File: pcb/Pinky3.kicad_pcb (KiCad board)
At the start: 2 copper layers, 137 x 100.9 mm, 67 parts, among them J1 MJ-4PP-9, P1 i2c-pin, P2 i2c-pin, SW1 RESET_SW, SW10 SW_PUSH, SW11 SW_PUSH, SW12 SW_PUSH, SW13 SW_PUSH, SW14 SW_PUSH, SW15 SW_PUSH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

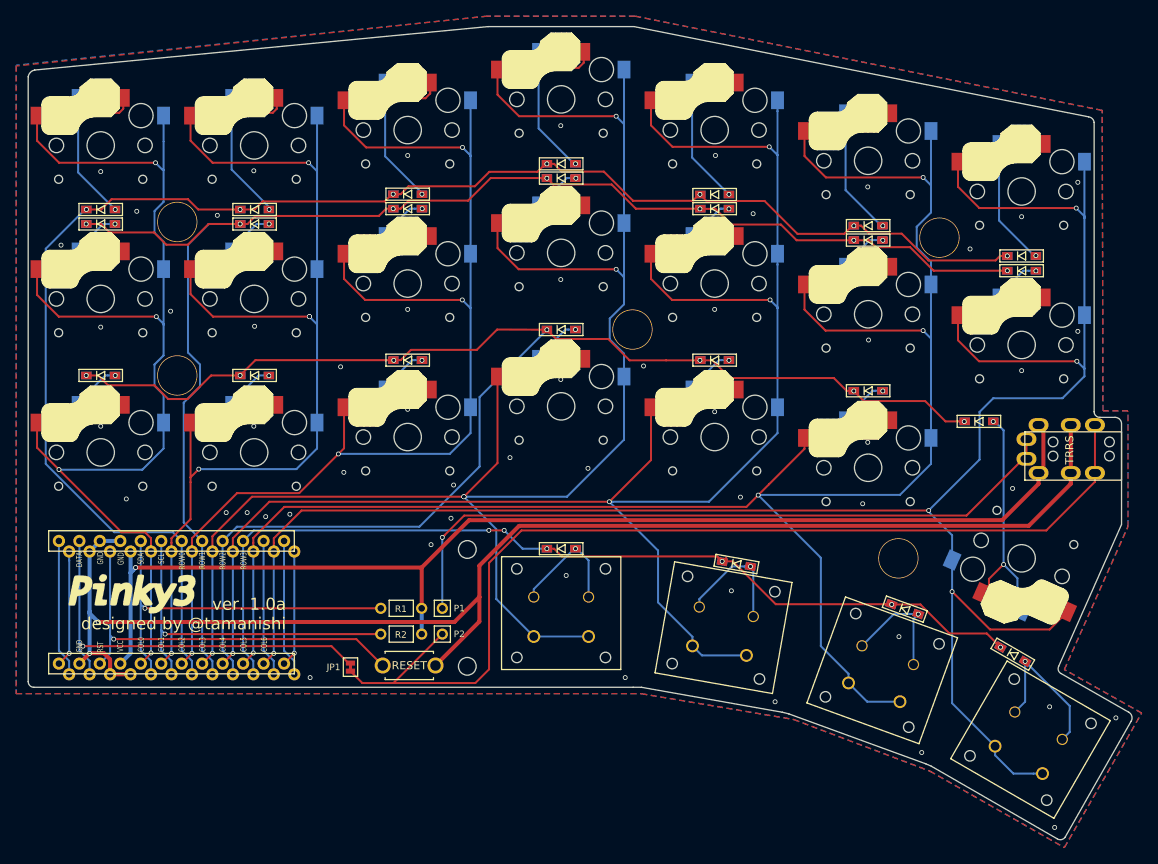
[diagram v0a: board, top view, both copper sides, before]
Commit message: - change thumb switches to Kailh PG1232.
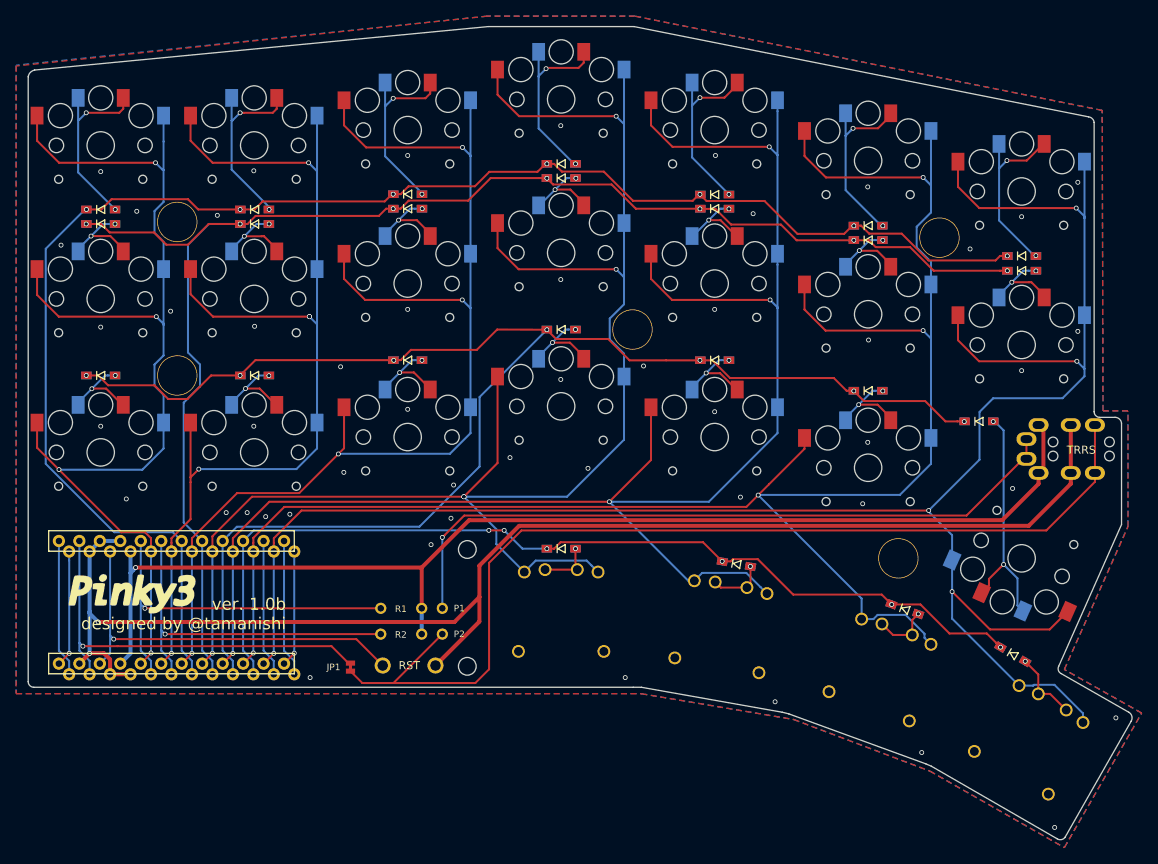
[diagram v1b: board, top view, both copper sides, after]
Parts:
- SW10, SW11, SW12, SW13, SW15, SW16, SW17, SW19, SW2, SW20, SW21, SW23, SW24, SW25, SW3, SW4, SW5, SW6, SW7, SW8, SW9: footprint kbd:Choc_Hotswap -> lib:Choc_Hotswap
- SW14, SW18, SW22, SW26: footprint lib:Kailh-PG1425-X-Switch-reversible -> lib:kailh_low_choc
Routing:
- net Net-(D25-Pad2): track 19.2 -> 9.00 mm
- net Net-(D17-Pad2): track 15.4 -> 7.03 mm
- net Net-(D13-Pad2): track 15.0 -> 7.03 mm
- net Net-(D21-Pad2): track 15.1 -> 7.24 mm
- net col3: track 204.8 -> 200.5 mm
- net col4: track 214.4 -> 210.1 mm
- net col5: track 232.2 -> 228.2 mm
- net col6: track 253.8 -> 250.1 mm
- net GND: vias 57 -> 53
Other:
- board text added: "ver. 1.0b designed by @tamanishi"
- board text removed: "ver. 1.0a designed by @tamanishi"

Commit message: supports choc v2
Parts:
- SW10, SW11, SW12, SW13, SW15, SW16, SW17, SW19, SW2, SW20, SW21, SW23, SW24, SW25, SW3, SW4, SW5, SW6, SW7, SW8, SW9: footprint lib:Choc_Hotswap -> lib:Choc_v2_Hotswap
- SW14, SW18, SW22, SW26: footprint lib:kailh_low_choc -> lib:Choc_v2_Hotswap
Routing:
- net col6: track 250.1 -> 271.8 mm, vias 5 -> 6
- net col3: track 200.5 -> 218.1 mm
- net col4: track 210.1 -> 225.8 mm, vias 4 -> 5
- net Net-(D13-Pad2): track 7.03 -> 22.1 mm, vias 1 -> 2
- net Net-(D21-Pad2): track 7.24 -> 22.1 mm, vias 1 -> 2
- net col5: track 228.2 -> 242.5 mm, vias 4 -> 5
- net Net-(D17-Pad2): track 7.03 -> 21.1 mm, vias 1 -> 2
- net Net-(D25-Pad2): track 9.00 -> 21.7 mm, vias 1 -> 2
- net Net-(D24-Pad2): track 29.8 -> 34.8 mm
- net col2: track 144.2 -> 145.4 mm
- net col1: track 130.7 -> 131.7 mm, vias 5 -> 4
- net GND: vias 53 -> 50
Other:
- board text added: "ver. 1.0c designed by @tamanishi"
- board text removed: "ver. 1.0b designed by @tamanishi"

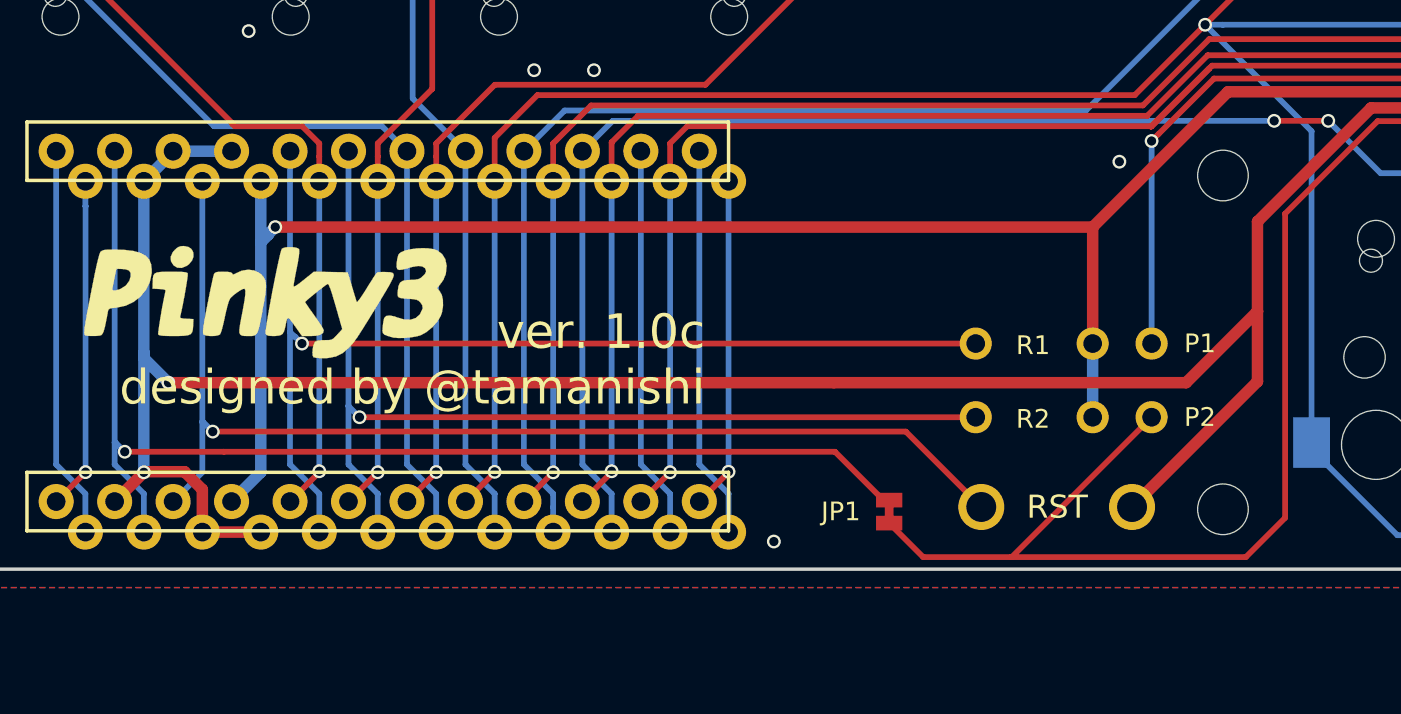
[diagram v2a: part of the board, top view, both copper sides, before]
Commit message: change horizontal reset switch
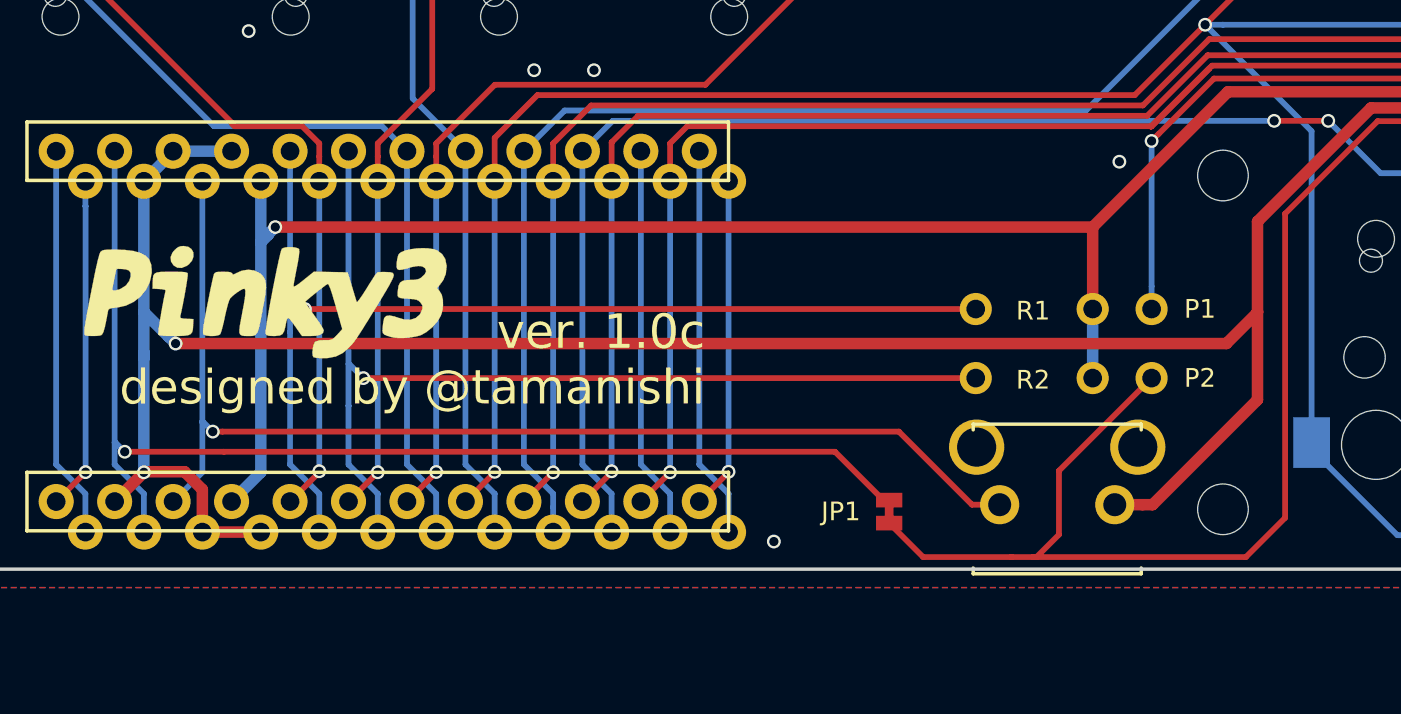
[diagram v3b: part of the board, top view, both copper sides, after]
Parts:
- SW1: footprint kbd:ResetSW -> lib:ResetSW_Horizontal; moved to B.Cu
- moved P2 1.70 mm to (92.4, 128.0)
- moved R2 1.70 mm to (87.3, 128.0)
- moved P1 1.50 mm to (92.4, 125.0)
- moved R1 1.50 mm to (87.3, 125.0)
- moved SW1 0.10 mm to (88.3, 133.5)
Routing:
- net VCC: track 147.8 -> 146.1 mm
- net Net-(J1-PadA): track 87.8 -> 86.3 mm
- net Net-(J1-PadB): track 127.2 -> 128.6 mm
- net reset: track 49.8 -> 50.6 mm
- net GND: track 176.0 -> 176.6 mm
